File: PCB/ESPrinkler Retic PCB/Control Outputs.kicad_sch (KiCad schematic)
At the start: 126 parts, among them Q10 AO3400A, Q11 AO3400A, Q3 AO3400A, Q4 AO3400A, Q5 AO3400A, Q6 AO3400A, Q7 AO3400A, Q8 AO3400A, Q9 AO3400A, U10 MOC3063S, U2 MOC3063S, U3 MOC3063S, U4 MOC3063S, U5 MOC3063S, U6 MOC3063S, U7 MOC3063S, U8 MOC3063S, U9 MOC3063S

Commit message: Continue PCB design
Change footprint of triacs to include solder tab for securing package to PCB and heat dissipation.

Change footprint of optocoupler for better solder mask outlines and smaller pads.
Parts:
- D14, D15, D16, D17, D4, D5, D6, D7, D8: footprint Package_TO_SOT_THT:TO-220-3_Horizontal_TabDown -> Footprints:TO-220-3_Horizontal_TabDown_Solder
- U10, U2, U3, U4, U5, U6, U7, U8, U9: footprint Footprints:MOC306XS_LTO-M -> Footprints:MOC306XS_LTO
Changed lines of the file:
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@@
 			)
 		)
-		(property "Footprint" "Package_TO_SOT_THT:TO-220-3_Horizontal_TabDown"
+		(property "Footprint" "Footprints:TO-220-3_Horizontal_TabDown_Solder"
 			(at 182.245 73.025 90)
 			(effects
@@
 			)
 		)
-		(property "Footprint" "Footprints:MOC306XS_LTO-M"
+		(property "Footprint" "Footprints:MOC306XS_LTO"
 			(at 224.79 76.2 0)
 			(effects
@@
 			)
 		)
-		(property "Footprint" "Footprints:MOC306XS_LTO-M"
+		(property "Footprint" "Footprints:MOC306XS_LTO"
 			(at 88.9 185.42 0)
 			(effects
@@
 			)
 		)
-		(property "Footprint" "Footprints:MOC306XS_LTO-M"
+		(property "Footprint" "Footprints:MOC306XS_LTO"
 			(at 88.9 148.59 0)
 			(effects
@@
 			)
 		)
-		(property "Footprint" "Footprints:MOC306XS_LTO-M"
+		(property "Footprint" "Footprints:MOC306XS_LTO"
 			(at 88.9 113.03 0)
 			(effects
@@
 			)
 		)
-		(property "Footprint" "Footprints:MOC306XS_LTO-M"
+		(property "Footprint" "Footprints:MOC306XS_LTO"
 			(at 88.9 41.91 0)
 			(effects
@@
 			)
 		)
-		(property "Footprint" "Package_TO_SOT_THT:TO-220-3_Horizontal_TabDown"
+		(property "Footprint" "Footprints:TO-220-3_Horizontal_TabDown_Solder"
 			(at 182.245 109.855 90)
 			(effects
@@
 			)
 		)
-		(property "Footprint" "Package_TO_SOT_THT:TO-220-3_Horizontal_TabDown"
+		(property "Footprint" "Footprints:TO-220-3_Horizontal_TabDown_Solder"
 			(at 46.355 109.855 90)
 			(effects
@@
 			)
 		)
-		(property "Footprint" "Package_TO_SOT_THT:TO-220-3_Horizontal_TabDown"
+		(property "Footprint" "Footprints:TO-220-3_Horizontal_TabDown_Solder"
 			(at 46.355 73.025 90)
 			(effects
@@
 			)
 		)
-		(property "Footprint" "Footprints:MOC306XS_LTO-M"
+		(property "Footprint" "Footprints:MOC306XS_LTO"
 			(at 224.79 113.03 0)
 			(effects
@@
 			)
 		)
-		(property "Footprint" "Package_TO_SOT_THT:TO-220-3_Horizontal_TabDown"
+		(property "Footprint" "Footprints:TO-220-3_Horizontal_TabDown_Solder"
 			(at 46.355 38.735 90)
 			(effects
@@
 			)
 		)
-		(property "Footprint" "Package_TO_SOT_THT:TO-220-3_Horizontal_TabDown"
+		(property "Footprint" "Footprints:TO-220-3_Horizontal_TabDown_Solder"
 			(at 46.355 145.415 90)
 			(effects
@@
 			)
 		)
-		(property "Footprint" "Footprints:MOC306XS_LTO-M"
+		(property "Footprint" "Footprints:MOC306XS_LTO"
 			(at 224.79 41.91 0)
 			(effects
@@
 			)
 		)
-		(property "Footprint" "Footprints:MOC306XS_LTO-M"
+		(property "Footprint" "Footprints:MOC306XS_LTO"
 			(at 88.9 76.2 0)
 			(effects
@@
 			)
 		)
-		(property "Footprint" "Package_TO_SOT_THT:TO-220-3_Horizontal_TabDown"
+		(property "Footprint" "Footprints:TO-220-3_Horizontal_TabDown_Solder"
 			(at 46.355 182.245 90)
 			(effects
@@
 			)
 		)
-		(property "Footprint" "Package_TO_SOT_THT:TO-220-3_Horizontal_TabDown"
+		(property "Footprint" "Footprints:TO-220-3_Horizontal_TabDown_Solder"
 			(at 182.245 145.415 90)
 			(effects
@@
 			)
 		)
-		(property "Footprint" "Package_TO_SOT_THT:TO-220-3_Horizontal_TabDown"
+		(property "Footprint" "Footprints:TO-220-3_Horizontal_TabDown_Solder"
 			(at 182.245 38.735 90)
 			(effects
@@
 			)
 		)
-		(property "Footprint" "Footprints:MOC306XS_LTO-M"
+		(property "Footprint" "Footprints:MOC306XS_LTO"
 			(at 224.79 148.59 0)
 			(effects

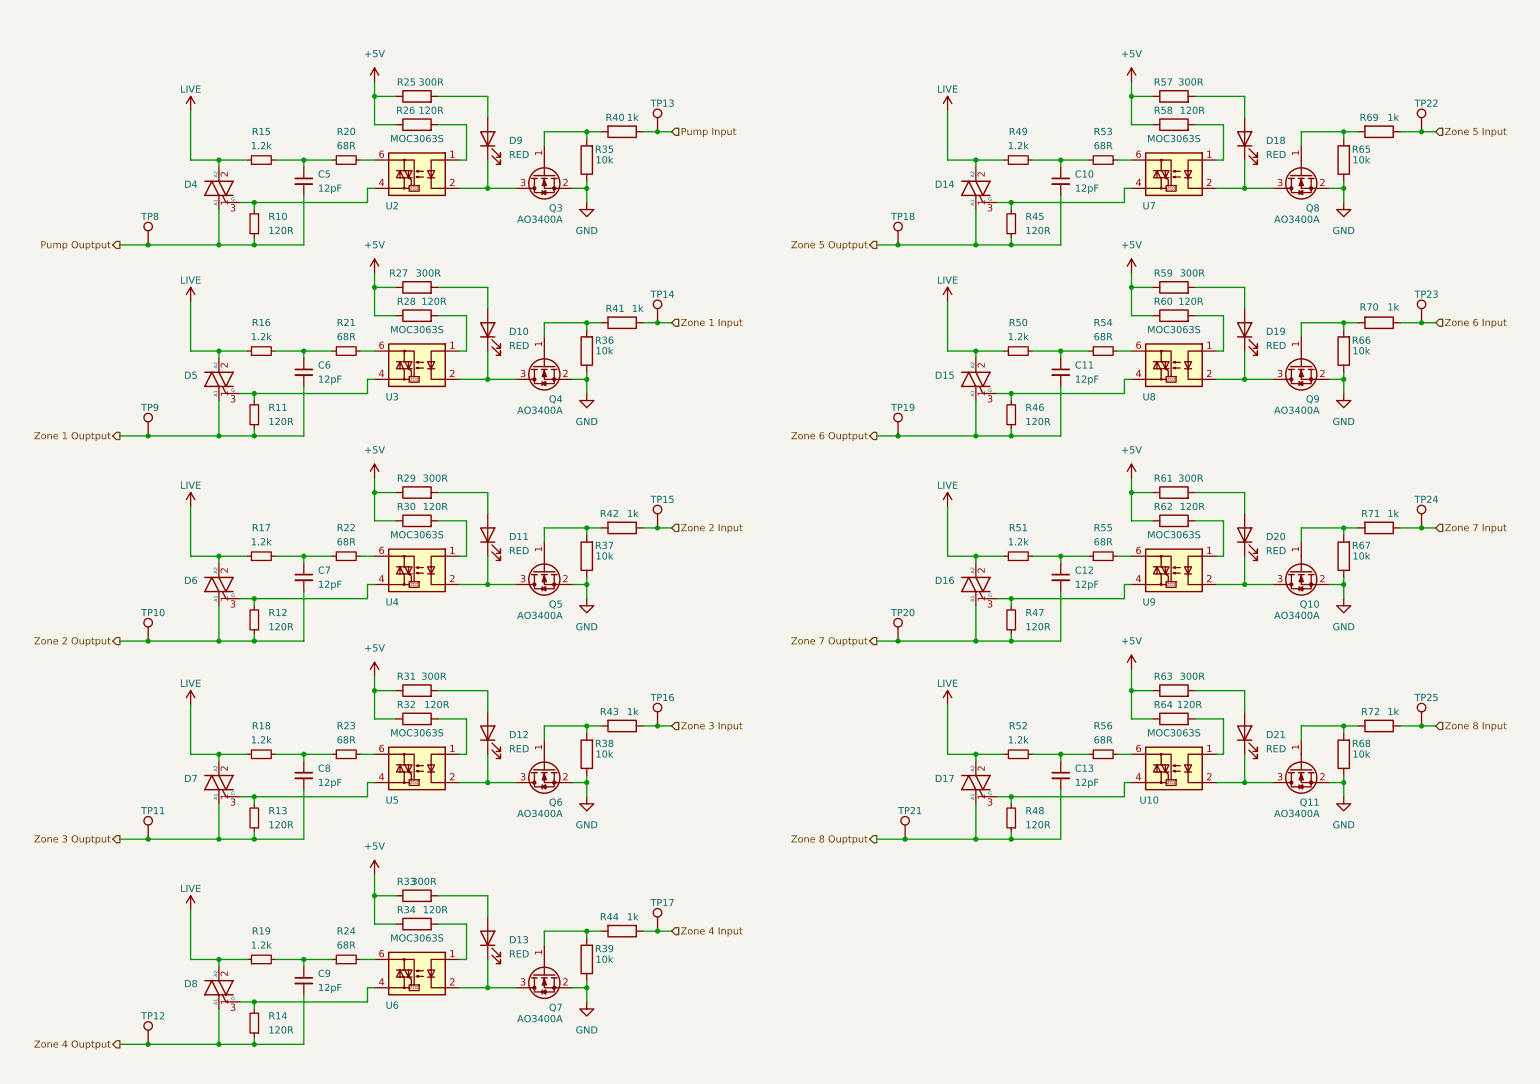
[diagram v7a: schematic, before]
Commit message: Change LED output indicator
Change LED indication for each channel to be powered off 24VAC line post triac instead of off the MOSFET. Easier PCB design and effectively same result
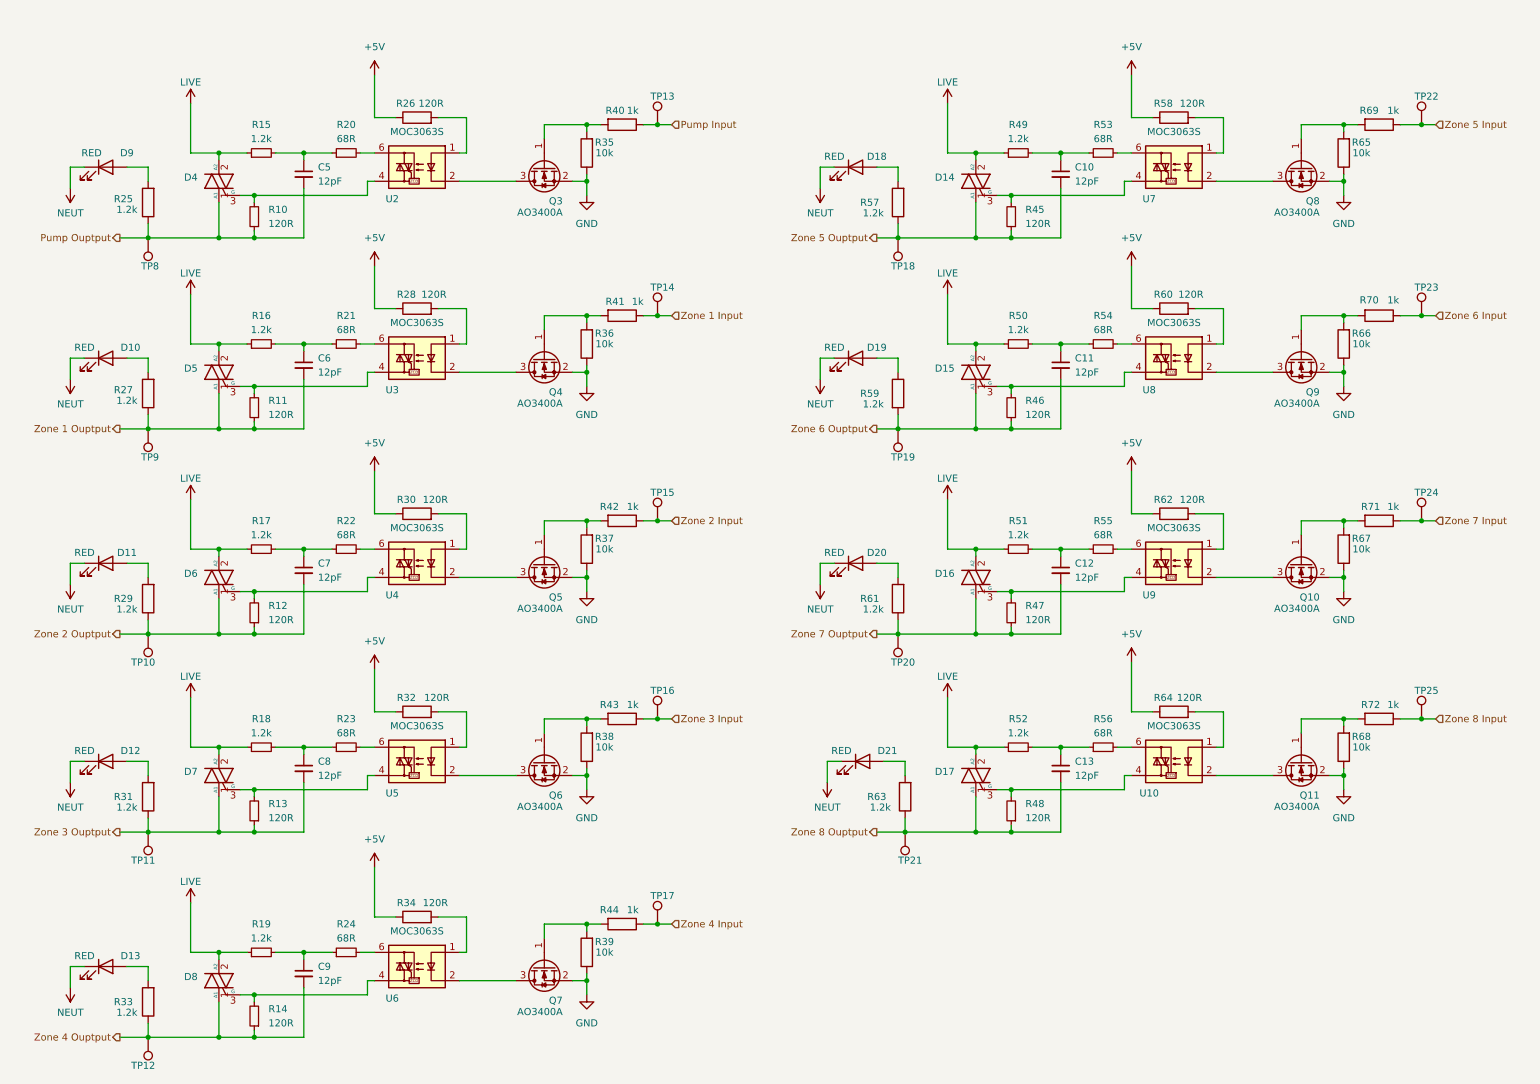
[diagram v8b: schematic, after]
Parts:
- R25, R27, R29, R31, R33, R57, R59, R61, R63: value 300R -> 1.2k; Manufacturer P/N 0805W8F3000T5E -> 0805W8F1201T5E; Supplier P/N C17617 -> C17379
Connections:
- net +5V: no longer R25.1, R27.1, R29.1, R31.1, R33.1, R57.1, R59.1, R61.1, R63.1
- net Pump Ouptput: now also R25.1
- net Zone 1 Ouptput: now also R27.1
- net Zone 2 Ouptput: now also R29.1
- net Zone 3 Ouptput: now also R31.1
- net Zone 4 Ouptput: now also R33.1
- net Zone 5 Ouptput: now also R57.1
- net Zone 6 Ouptput: now also R59.2
- net Zone 7 Ouptput: now also R61.1
- net Zone 8 Ouptput: now also R63.1
- net at Q9.3 (D), U8.2: no longer D19.1 (K)
- net at Q7.3 (D), U6.2: no longer D13.1 (K)
- net at Q6.3 (D), U5.2: no longer D12.1 (K)
- net at Q5.3 (D), U4.2: no longer D11.1 (K)
- net at Q3.3 (D), U2.2: no longer D9.1 (K)
- net at Q8.3 (D), U7.2: no longer D18.1 (K)
- net at Q11.3 (D), U10.2: no longer D21.1 (K)
- net at Q10.3 (D), U9.2: no longer D20.1 (K)
- net at D19.2 (A): now also R59.1; no longer R59.2
- net at Q4.3 (D), U3.2: no longer D10.1 (K)
- new net NEUT: D10.1 (K), D11.1 (K), D12.1 (K), D13.1 (K), D18.1 (K), D19.1 (K), D20.1 (K), D21.1 (K), D9.1 (K)
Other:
- moved on the sheet: C10, C11, C12, C13, C5, C6, C7, C8, C9, D10, D11, D12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
